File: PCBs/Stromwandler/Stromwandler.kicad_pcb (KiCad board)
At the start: 2 copper layers, 30 x 30 mm, 10 parts, among them IC1 HO10-P_SP33, J1 Conn_02x05_Odd_Even, J4 2X

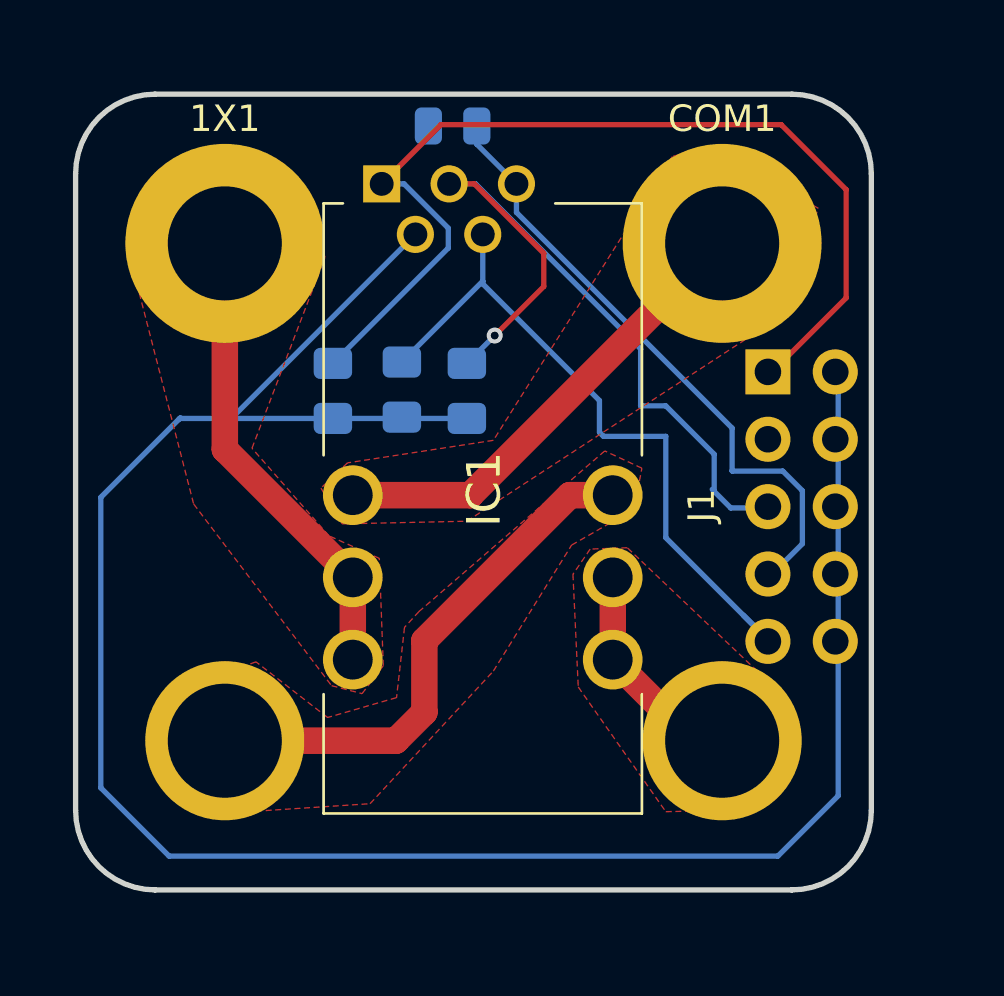
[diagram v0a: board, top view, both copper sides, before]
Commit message: Anpassungen
GND Fill und Tausch von Signal und Leistungsseite
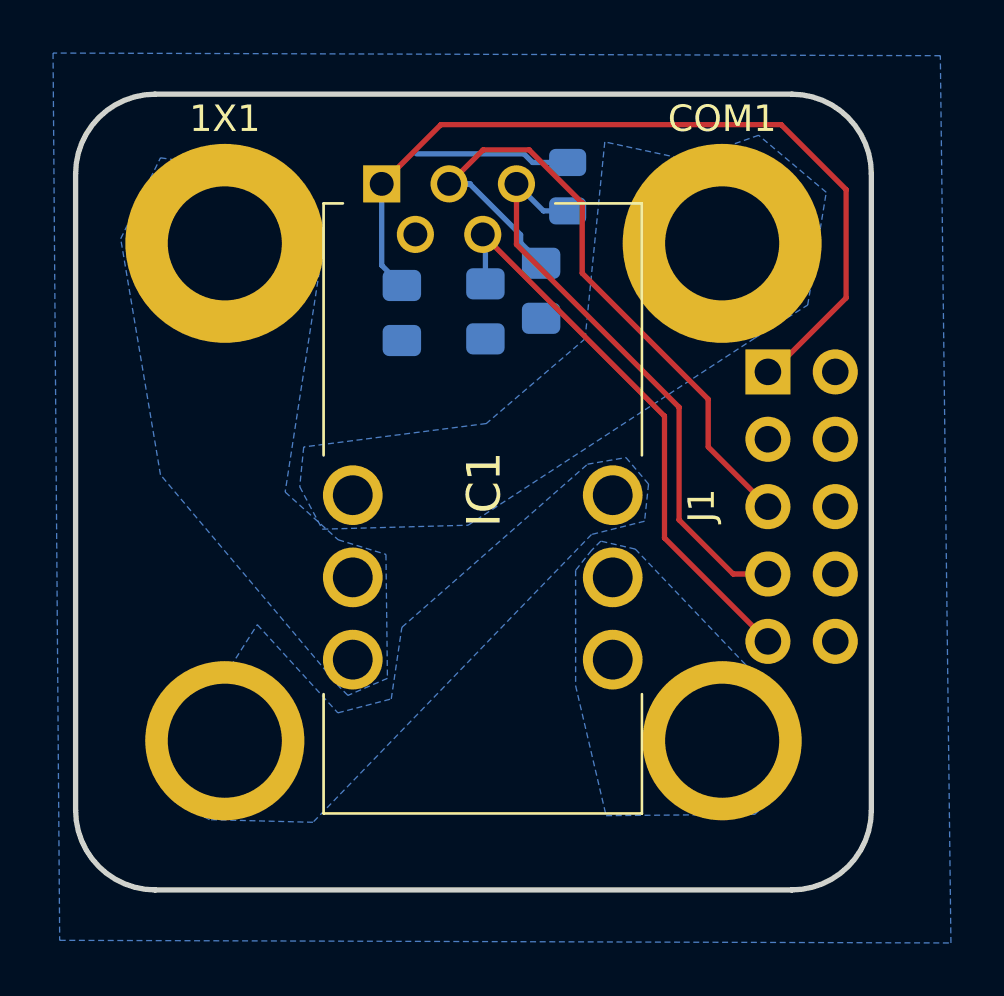
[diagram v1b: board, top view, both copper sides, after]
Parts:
- moved R1 4.90 mm to (103.5, 88.5), turned to 90 degrees
- moved C1 4.70 mm to (102.5, 92.4)
- moved C3 4.32 mm to (100.5, 93.2)
- moved C2 3.92 mm to (97.3, 93.2)
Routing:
- net Net-(IC1-0V): track 81.6 -> 0.00 mm
- net Net-(3X1-Pin_1): track 20.0 -> 0.47 mm
- net Net-(COM1-Pin_1): track 19.4 -> 1.59 mm
- net Net-(1X1-Pin_1): track 19.3 -> 1.59 mm
- net Net-(IC1-RETENTION_PIN_4): track 8.49 -> 1.07 mm
- net Net-(IC1-VREF_(IN/OUT)): track 27.0 -> 21.7 mm
- net Net-(IC1-VOUT): track 29.4 -> 26.4 mm, vias 1 -> 0
- net Net-(IC1-OCD): track 23.6 -> 21.8 mm
- net Net-(IC1-+UC): track 40.6 -> 39.6 mm
- added copper zone on B.Cu, net Net-(1X1-Pin_1)
- added copper zone on B.Cu, net Net-(3X1-Pin_1)
- added copper zone on B.Cu, net Net-(COM1-Pin_1)
- added copper zone on B.Cu, net Net-(IC1-0V)
- added copper zone on B.Cu, net Net-(IC1-RETENTION_PIN_4)
- removed copper zone on F.Cu, net Net-(1X1-Pin_1)
- removed copper zone on F.Cu, net Net-(3X1-Pin_1)
- removed copper zone on F.Cu, net Net-(COM1-Pin_1)
- removed copper zone on F.Cu, net Net-(IC1-RETENTION_PIN_4)

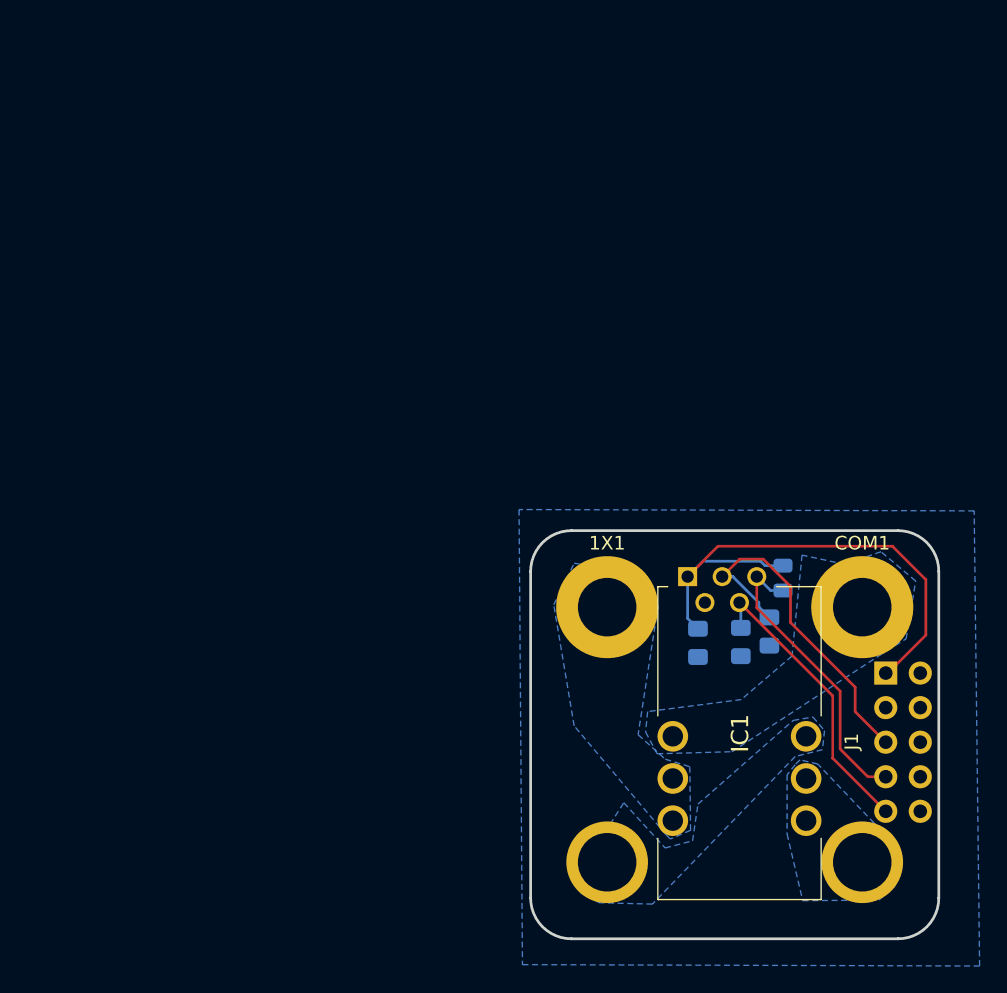
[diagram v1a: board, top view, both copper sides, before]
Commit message: Test with smaller holes, bottom only; to avoid DRC errors
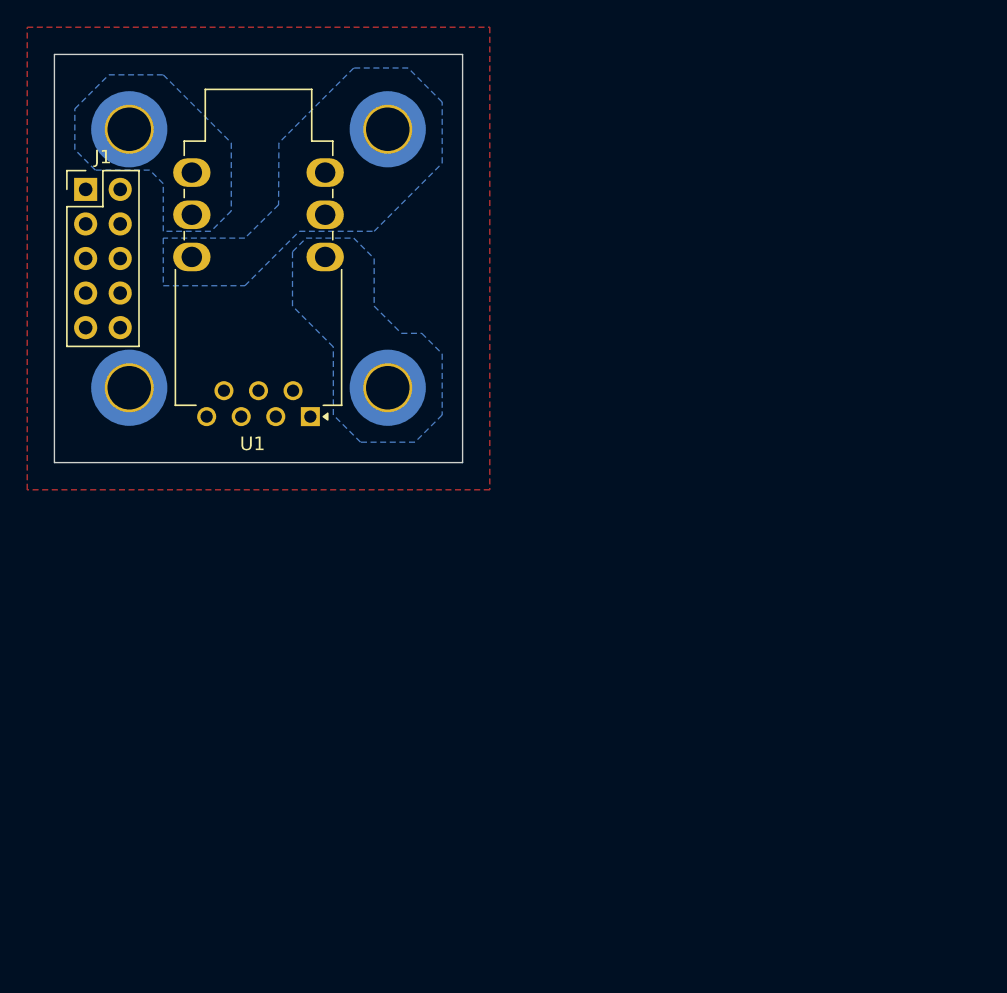
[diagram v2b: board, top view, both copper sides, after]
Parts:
- removed 1X1, 3X1, COM1: Conn_01x01, MountingHole:MountingHole_4.3mm_M4_DIN965_Pad
- removed C1, C2, C3: 47n, Capacitor_SMD:C_0805_2012Metric_Pad1.18x1.45mm_HandSolder
- removed IC1: HO10-P_SP33, HO10_P_SP33:HO10PSP33
- removed J4: 2X, MountingHole:MountingHole_4.3mm_M4_DIN965_Pad
- removed R1: 50k, Resistor_SMD:R_0805_2012Metric
- added H1: MountingHole_Pad, MountingHole:MountingHole_3.2mm_M3_DIN965_Pad_TopOnly, B.Cu at (55.5, 55.5)
- added H2: MountingHole_Pad, MountingHole:MountingHole_3.2mm_M3_DIN965_Pad_TopOnly, B.Cu at (74.5, 55.5)
- added H3: MountingHole_Pad, MountingHole:MountingHole_3.2mm_M3_DIN965_Pad_TopOnly, B.Cu at (55.5, 74.5)
- added H4: MountingHole_Pad, MountingHole:MountingHole_3.2mm_M3_DIN965_Pad_TopOnly, B.Cu at (74.5, 74.5)
- added U1: HO15-NPxSP33, Sensor_Current:LEM_HO8-NP, F.Cu at (68.8, 76.6)
- moved J1 68.8 mm to (52.3, 59.9)
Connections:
- J1 pad 1: Net-(IC1-+UC) -> unconnected-(J1-Pin_1-Pad1)
- J1 pad 10: Net-(IC1-0V) -> unconnected-(J1-Pin_10-Pad10)
- J1 pad 2: Net-(IC1-0V) -> unconnected-(J1-Pin_2-Pad2)
- J1 pad 4: Net-(IC1-0V) -> unconnected-(J1-Pin_4-Pad4)
- J1 pad 5: Net-(IC1-VOUT) -> unconnected-(J1-Pin_5-Pad5)
- J1 pad 6: Net-(IC1-0V) -> unconnected-(J1-Pin_6-Pad6)
- J1 pad 7: Net-(IC1-OCD) -> unconnected-(J1-Pin_7-Pad7)
- J1 pad 8: Net-(IC1-0V) -> unconnected-(J1-Pin_8-Pad8)
- J1 pad 9: Net-(IC1-VREF_(IN/OUT)) -> unconnected-(J1-Pin_9-Pad9)
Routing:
- net Net-(IC1-+UC): track 39.6 -> 0.00 mm
- net Net-(IC1-VOUT): track 26.4 -> 0.00 mm
- net Net-(IC1-OCD): track 21.8 -> 0.00 mm
- net Net-(IC1-VREF_(IN/OUT)): track 21.7 -> 0.00 mm
- net Net-(1X1-Pin_1): track 1.59 -> 0.00 mm
- net Net-(COM1-Pin_1): track 1.59 -> 0.00 mm
- net Net-(IC1-RETENTION_PIN_4): track 1.07 -> 0.00 mm
- added copper zone on F.Cu, net GND
- added copper zone on B.Cu, net Net-(U1-IN1)
- added copper zone on B.Cu, net Net-(U1-IN2)
- added copper zone on B.Cu, net Net-(U1-OUT1)
- removed copper zone on B.Cu, net Net-(1X1-Pin_1)
- removed copper zone on B.Cu, net Net-(3X1-Pin_1)
- removed copper zone on B.Cu, net Net-(COM1-Pin_1)
- removed copper zone on B.Cu, net Net-(IC1-0V)
- removed copper zone on B.Cu, net Net-(IC1-RETENTION_PIN_4)
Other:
- outline, holes or cut-outs redrawn
